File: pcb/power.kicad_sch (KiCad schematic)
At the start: 0 parts

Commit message: Add TI buck converter to power
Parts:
- added C21: 100n, Capacitor_SMD:C_0603_1608Metric, symbol Device:C_Small
- added J3: XT30PW-M, Connector_AMASS:AMASS_XT30PW-M_1x02_P2.50mm_Horizontal, symbol Connector:Conn_01x02_Pin
- added J4: Screw_Terminal_01x02, Wurth_ScrewTerminal_691137710002:Wurth_ScrewTerminal_691137710002, symbol Connector:Screw_Terminal_01x02
- added Q2: NTR4003N, Package_TO_SOT_SMD:SOT-23-3, symbol Transistor_FET:Q_NMOS_GSD
- added R11, R12, R15, R16: 47k, Resistor_SMD:R_0603_1608Metric, symbol Device:R_Small_US
- added R17: PE1206FKM470R005Z, Resistor_SMD:R_1206_3216Metric, symbol Device:R_Small_US
- added U4: LM66200, Package_TO_SOT_SMD:SOT-583-8, symbol LM66200:LM66200
- added U5: ZXCT180B3W5, Package_TO_SOT_SMD:SOT-23-5, symbol DI_ZXCT180:ZXCT180B2
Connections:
- new net: R15.1, U4.4 (~{ON})
- new net +3V3: C21.1, R16.1, U5.5 (VS)
- new net +5V: U4.2 (VOUT), U4.7 (VOUT)
- new net +BATT: R17.2, U5.3 (IN-)
- new net BATT_MEAS: J4.1 (Pin_1), R11.1, R17.1, U5.1 (IN+)
- new net BATT_SENSE: R11.2, R12.1
- new net BATT_SW: J3.2 (Pin_2), J4.2 (Pin_2)
- new net BUCK_5V: U4.6 (VIN2)
- new net DIODE_STATUS: R16.2, U4.8 (ST)
- new net GND: C21.2, J3.1 (Pin_1), R12.2, R15.2, U4.1 (GND), U4.5 (GND), U5.2 (GND)
- new net I_SENSE: U5.4 (OUT)
- new net VBUS: U4.3 (VIN1)
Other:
- note added: "5mOhm 1W"
- note added: "7.4V Lithium ion battery"
- note added: "Battery current sense"
- note added: "Battery off-board switch"
- note added: "Cbypass"
- note added: "Ideal diode 5V source selector 2.5A max"
- note added: "Vout = (Iload * Rshunt) * GAIN GAIN = 100V/V Rshunt = 0.005 ohm Iload | Vout 100mA | 25mV 500mA | 125mV 1A | 250mV 5A | 1250mV 10A | 2500mV 13.2A | 3300mV"
- note added: "limit switch NC"
- note added: "we have a 12-bit ADC so 0V-3.3V = 0-4095 at least 1 count per millivolt"

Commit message: Begin power tree design
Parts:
- removed R15, R16: 47k, Resistor_SMD:R_0603_1608Metric, symbol Device:R_Small_US
- removed U4: LM66200, Package_TO_SOT_SMD:SOT-583-8, symbol LM66200:LM66200
- added C16, C17: 10u, symbol Device:C_Small
- added C18, C19: 100n, symbol Device:C_Small
- added C20: 47p, symbol Device:C_Small
- added C22: 22u, symbol Device:C_Small
- added L1: 2.2u, symbol Device:L_Small
- added R10: 30k, symbol Device:R_Small_US
- added R8: 47k, symbol Device:R_Small_US
- added R9: 135k, symbol Device:R_Small_US
- added U3: TPS561246DRLR, Package_TO_SOT_SMD:SOT-563, symbol TI_DCDC:TPS561246DRLR
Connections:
- net +3V3: now also C20.1, C22.1, L1.2, R9.1
- net GND: now also C16.2, C17.2, C18.2, C22.2, R10.2, U3.3 (GND)
- new net: C16.1, C17.1, C18.1, R8.1, U3.1 (VIN)
- new net: R8.2, U3.5 (EN)
- new net: C19.1, U3.4 (BST)
- new net: C19.2, L1.1, U3.2 (SW)
- new net: C20.2, R10.1, R9.2, U3.6 (FB)
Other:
- note added: "Cin C: 20 μF - 20 μF ESR: 1 mΩ - 20 mΩ Irms: 381 mA - 10 kA VDC: 10.92 V - 25 V"
- note added: "Cout Recommended Limits: C: 22 μF - 60 μF ESR: 1 mΩ - 20 mΩ Irms: 332.1 mA - 10 kA VDC: 4.95 V - 8 V"
- note added: "SW node inductor Recommended Limits: L: 1.5 μH - 4.7 μH DCR: 3.3 mΩ - 330 mΩ IDC: 1.35 A - 27.04 A"
- note removed: "Ideal diode 5V source selector 2.5A max"
- moved on the sheet: Q2

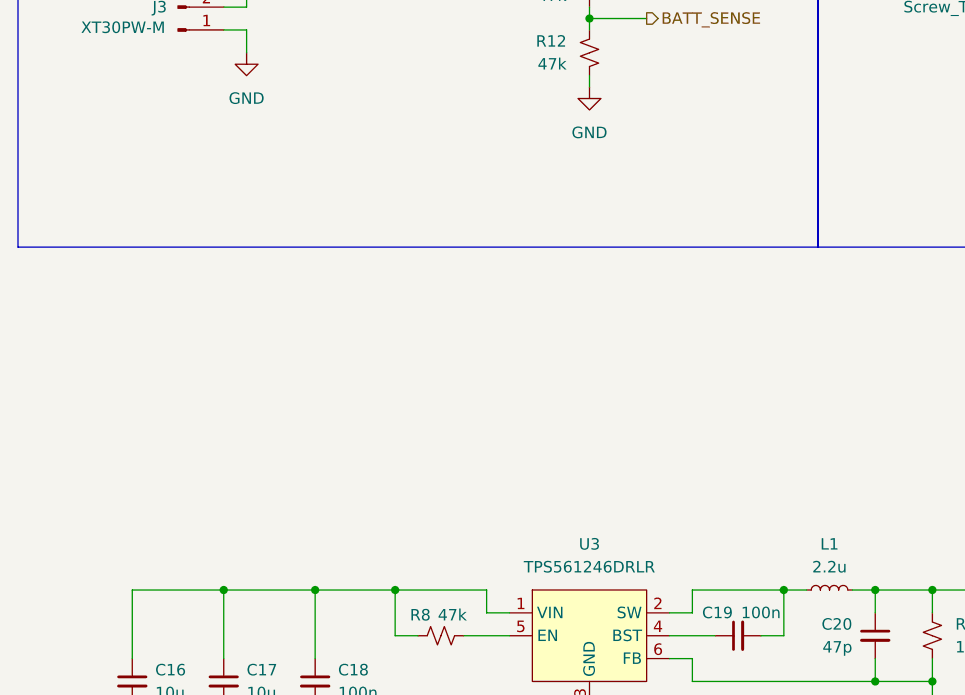
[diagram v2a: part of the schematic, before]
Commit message: Implement flash memory connection
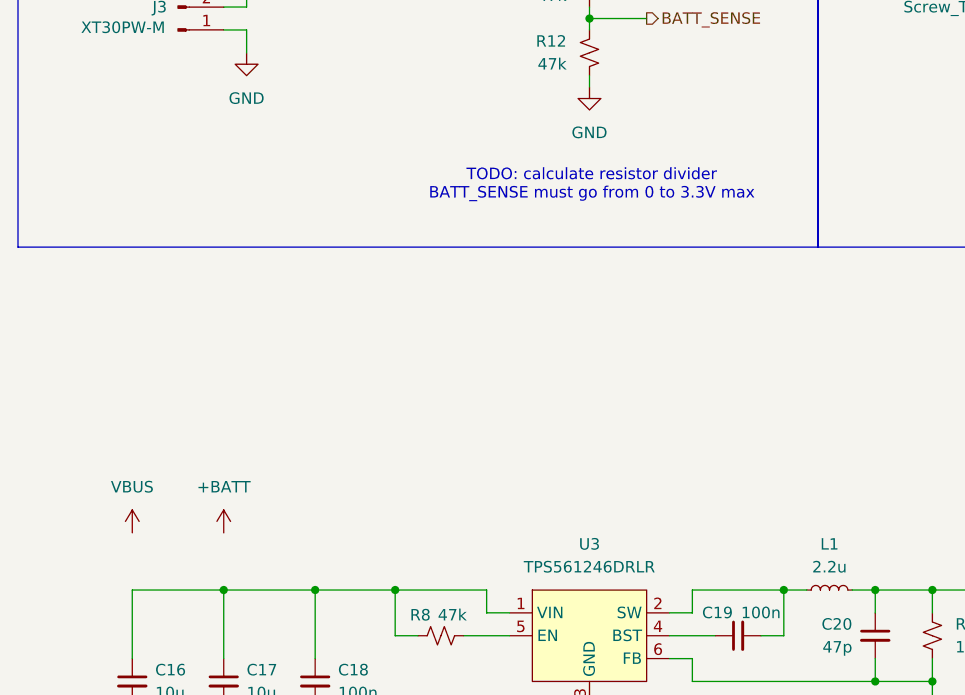
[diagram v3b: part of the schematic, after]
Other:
- note added: "TODO: calculate resistor divider BATT_SENSE must go from 0 to 3.3V max"
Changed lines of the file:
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@@
 		)
 	)
+	(text "TODO: calculate resistor divider\nBATT_SENSE must go from 0 to 3.3V max"
+		(exclude_from_sim no)
+		(at 76.454 92.964 0)
+		(effects
+			(font
+				(size 1.27 1.27)
+			)
+			(justify top)
+		)
+	)
 	(text "Vout = (Iload * Rshunt) * GAIN\nGAIN = 100V/V Rshunt = 0.005 ohm\nIload | Vout\n100mA | 25mV\n500mA | 125mV\n1A    | 250mV\n5A    | 1250mV\n10A   | 2500mV\n13.2A | 3300mV"
 		(exclude_from_sim no)
@@
 			"lQcAgBRhagokz4033rh///5zVxobGxN+vRkAAP52TE2B5MnNzZ09e/a5Kzk5XoUAADA1BQAAILSs"
 			"0AEAAADIdKopAAAAgammAAAABKaaAgAAEJhqCgAAQGCqKQAAAIGppgAAAASmmgIAABCYagoAAEBg"
-			"qikAAACBqaYAAAAEppoCAAAQmGoKAABAYP8FmIdzdeukvC0AAAAASUVORK5CYII="
+			"qikAAACBqaYAAAAEppoCAAAQmGoKAABAYP8FmIdzdeukvC0AAAAASUVORK5CYIIAAAAAAwAAAAAA"
+			"AAAAEB02oAEAAAEAAAAAAAAAAAAAAAAAAACzjGX6ABgFgAAAAAAAAAAAAwAAAAAAAAAgDx02oAEA"
+			"AAEAAAAAAAAAAAAAAAAAAAC2jGj6ABkFgAAAAAAAAAAAAwAAAAAAAADADh02oAEAAAEAAAAAAAAA"
+			"AAAAAAAAAAC1jG/6ABoFgAAAAAAAAAAACAAAAAAAAADwWAI2oAEAAAEAAAAAAAAAAAAAAAAAAACI"
+			"jFL6ABsFgAAAAAAAAAAAAwAAAAAAAAAgmBY2oAEAAAEAAAAAAAAAAAAAAAAAAACPjFH6ABwFgAAA"
+			"AAAAAAAAAwAAAAAAAABwyQY2oAEAAAEAAAAAAAAAAAAAAAAAAACCjFT6AB0FgAAAAAAAAAAAAwAA"
+			"AAAAAADw3Bw2oAEAAAEAAAAAAAAAAAAAAAAAAACBjFv6AB4FgIDUHDagAQAAAwAAAAAAAACwzAY2"
+			"oAEAAAEAAAAAAAAAAAAAAAAAAACEjF76AB8FgAAAAAAAAAAAAwAAAAAAAADwVQI2oAEAAAEAAAAA"
+			"AAAAAAAAAAAAAACbjF36ACAFgMDZHDagAQAAAwAAAAAAAADQzAY2oAEAAAEAAAAAAAAAAAAAAAAA"
+			"AACejED6ACEFgODRHDagAQAAAwAAAAAAAAAQDh02oAEAAAEAAAAAAAAAAAAAAAAAAACdjEf6ACIF"
+			"gEpldEJyYWluc01vbm8gTkYgRXh0cmFCb2xkAAAAAAAAAAAAAAAAAACQjEr6ACMFgAAAAAAAAAAA"
+			"AwAAAAAAAABw2Bw2oAEAAAEAAAAAAAAAAAAAAAAAAACXjEn6ACQFgEDYHDagAQAAAwAAAAAAAAAw"
+			"0QY2oAEAAAEAAAAAAAAAAAAAAAAAAABqjEz6ACUFgEpldEJyYWluc01vbm9OTCBORlAgVGhpbgAA"
+			"AAAAAAAAAAAAAAAAAABpjLP6ACYFgAAAAAAAAAAAAwAAAAAAAACwzgY2oAEAAAEAAAAAAAAAAAAA"
+			"AAAAAABsjLb6ACcFgEpldEJyYWluc01vbm8gTkYgRXh0cmFMaWdodAAAAAAAAAAAAAAAAABjjLX6"
+			"ACgFgADZHDagAQAAAwAAAAAAAABgFPU1oAEAAAEAAAAAAAAAAAAAAAAAAABmjLj6ACkFgAAAAAAA"
+			"AAAAAwAAAAAAAAAwDR02oAEAAAEAAAAAAAAAAAAAAAAAAABljL/6ACoFgAAAAAAAAAAAAwAAAAAA"
+			"AABADx02oAEAAAEAAAAAAAAAAAAAAAAAAAB4jKL6ACsFgAAAAAAAAAAABAAAAAAAAAABAAAAAAAA"
+			"AAEAAAAAAAAAAAAAAAAAAAB/jKH6ACwFgAAAAAAAAAAAAwAAAAAAAABwWgI2oA=="
 		)
 	)
@@
 	)
 	(symbol
+		(lib_id "power:+BATT")
+		(at 35.56 133.35 0)
+		(unit 1)
+		(exclude_from_sim no)
+		(in_bom yes)
+		(on_board yes)
+		(dnp no)
+		(fields_autoplaced yes)
+		(property "Reference" "#PWR042"
+			(at 35.56 137.16 0)
+			(effects
+				(font
+					(size 1.27 1.27)
+				)
+				(hide yes)
+			)
+		)
+		(property "Value" "+BATT"
+			(at 35.56 128.27 0)
+			(effects
+				(font
+					(size 1.27 1.27)
+				)
+			)
+		)
+		(property "Footprint" ""
+			(at 35.56 133.35 0)
+			(effects
+				(font
+					(size 1.27 1.27)
+				)
+				(hide yes)
+			)
+		)
+		(property "Datasheet" ""
+			(at 35.56 133.35 0)
+			(effects
+				(font
+					(size 1.27 1.27)
+				)
+				(hide yes)
+			)
+		)
+		(property "Description" "Power symbol creates a global label with name \"+BATT\""
+			(at 35.56 133.35 0)
+			(effects
+				(font
+					(size 1.27 1.27)
+				)
+				(hide yes)
+			)
+		)
+		(pin "1"
+		)
+		(instances
+			(project ""
+				(path "/1f4fd4ed-9886-4375-a5ac-dc32d5760936/3ce152e6-c1c9-4db1-8237-913c82724d53"
+					(reference "#PWR042")
+					(unit 1)
+				)
+			)
+		)
+	)
+	(symbol
 		(lib_id "power:+3V3")
 		(at 127 137.16 0)
@@
 					(unit 1)
 				)
+			)
+		)
+	)
+	(symbol
+		(lib_id "power:VBUS")
+		(at 25.4 133.35 0)
+		(unit 1)
+		(exclude_from_sim no)
+		(in_bom yes)
+		(on_board yes)
+		(dnp no)
+		(fields_autoplaced yes)
+		(property "Reference" "#PWR041"
+			(at 25.4 137.16 0)
+			(effects
+				(font
+					(size 1.27 1.27)
+				)
+				(hide yes)
+			)
+		)
+		(property "Value" "VBUS"
+			(at 25.4 128.27 0)
+			(effects
+				(font
+					(size 1.27 1.27)
+				)
+			)
+		)
+		(property "Footprint" ""
+			(at 25.4 133.35 0)
+			(effects
+				(font
+					(size 1.27 1.27)
+				)
+				(hide yes)
+			)
+		)
+		(property "Datasheet" ""
+			(at 25.4 133.35 0)
+			(effects
+				(font
+					(size 1.27 1.27)
+				)
+				(hide yes)
+			)
+		)
+		(property "Description" "Power symbol creates a global label with name \"VBUS\""
+			(at 25.4 133.35 0)
+			(effects
+				(font
+					(size 1.27 1.27)
+				)
+				(hide yes)
+			)
+		)
+		(pin "1"
+		)
+		(instances
+			(project ""
+				(path "/1f4fd4ed-9886-4375-a5ac-dc32d5760936/3ce152e6-c1c9-4db1-8237-913c82724d53"
+					(reference "#PWR041")
+					(unit 1)
+				)

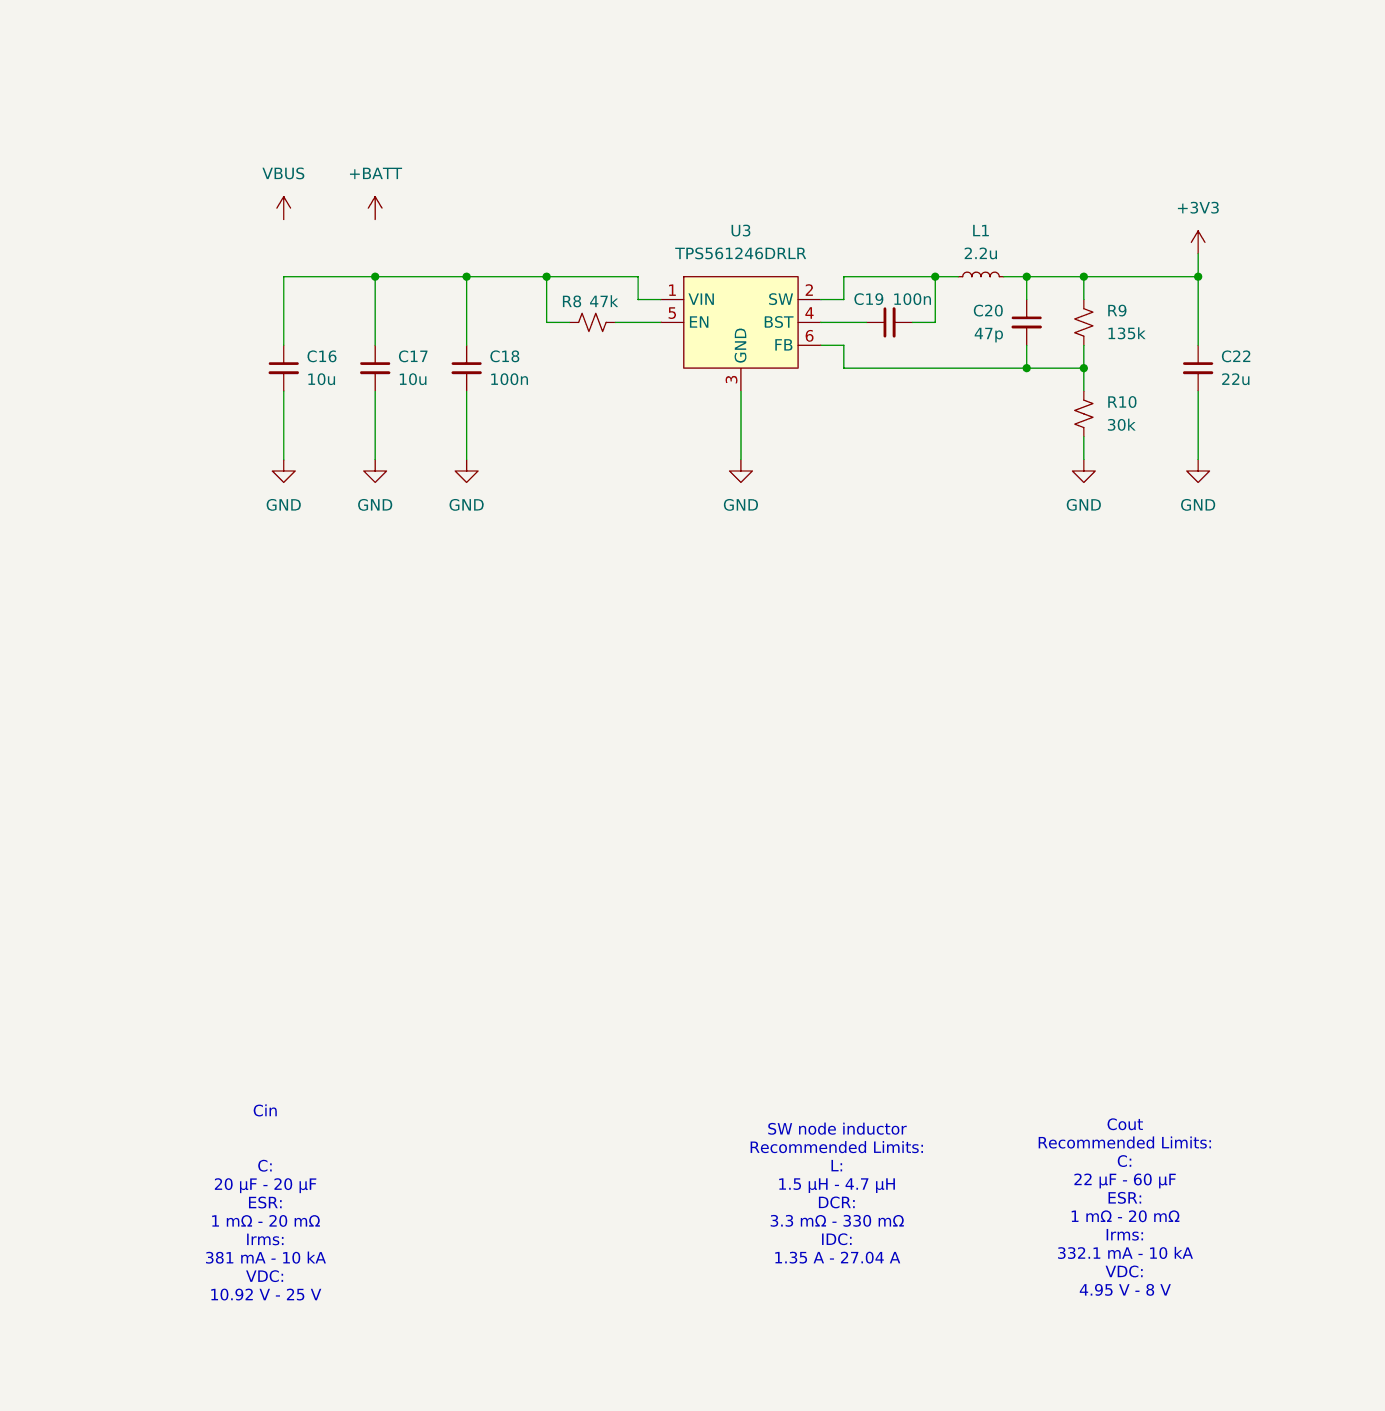
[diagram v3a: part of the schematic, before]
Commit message: Add comments for buck passives
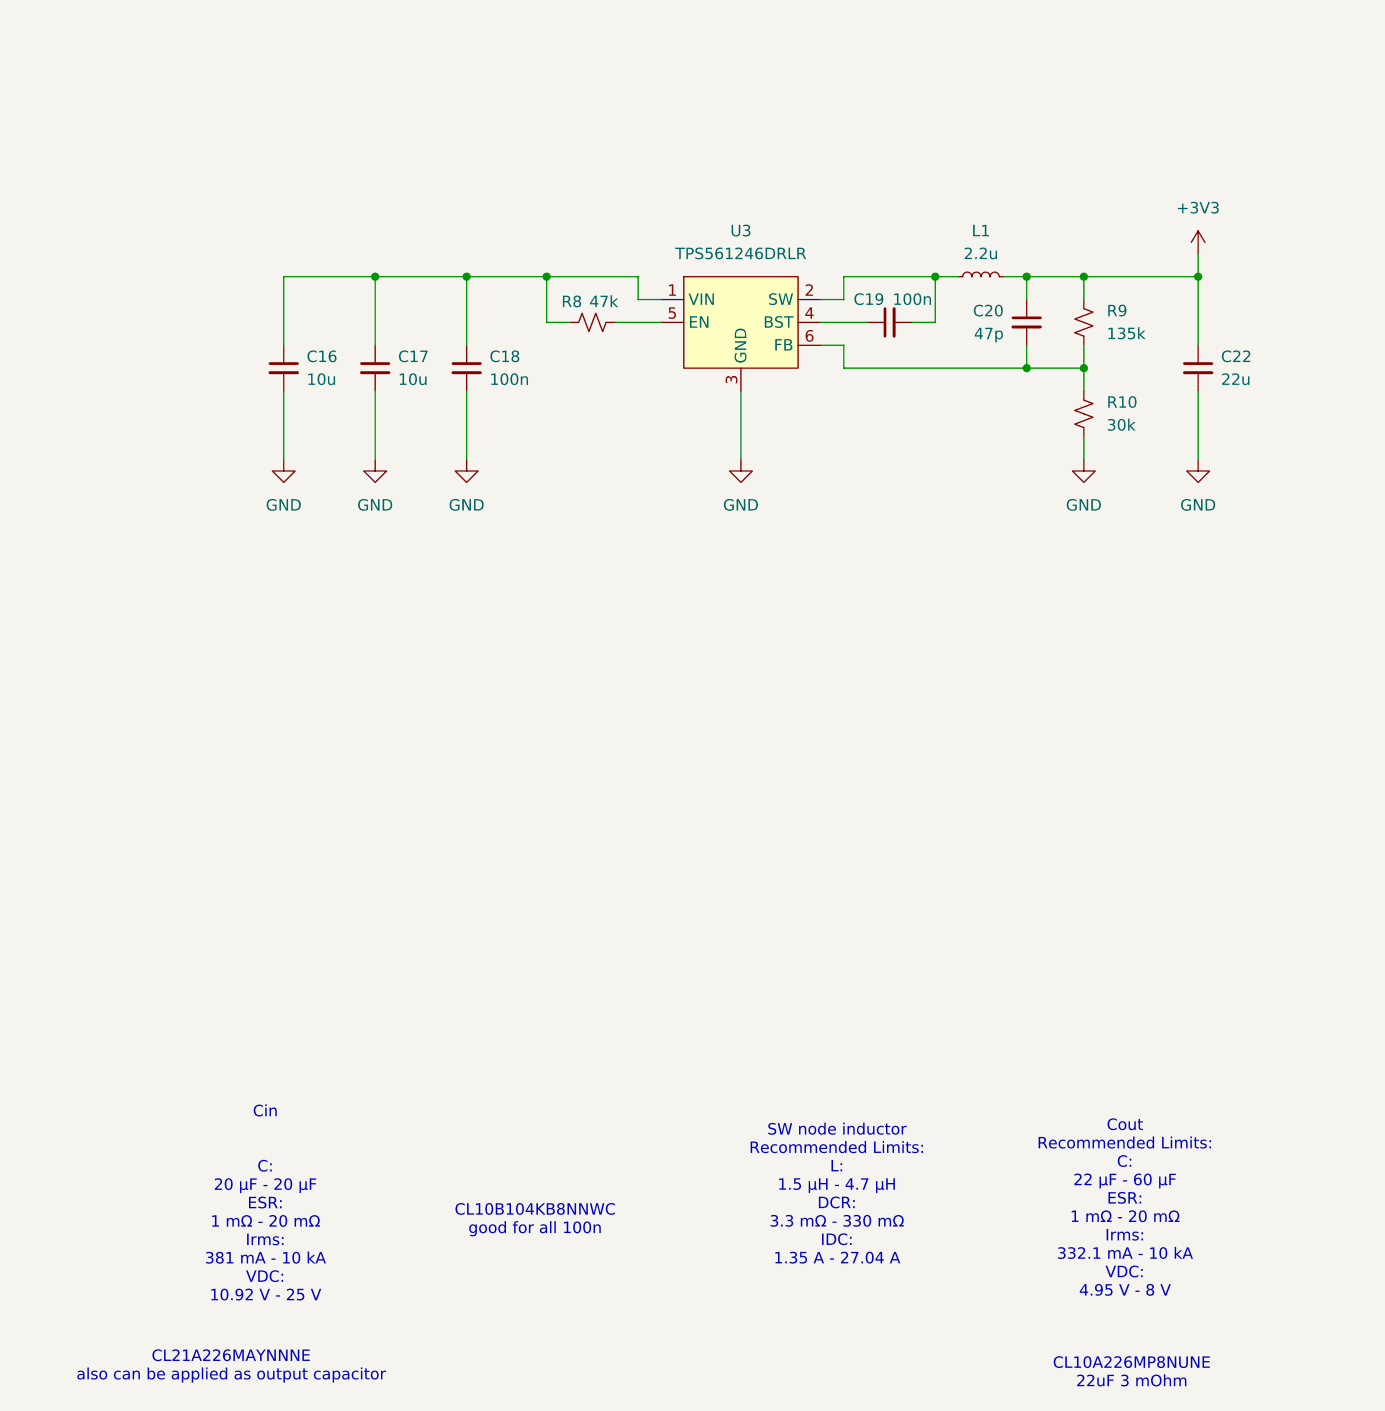
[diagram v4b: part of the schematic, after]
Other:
- note added: "CL10A226MP8NUNE 22uF 3 mOhm"
- note added: "CL10B104KB8NNWC good for all 100n"
- note added: "CL21A226MAYNNNE also can be applied as output capacitor"
